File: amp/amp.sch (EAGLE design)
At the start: 77 parts, among them IC1 OPA2134PA, Q1 BC547, Q10 IRF540, Q11 BC556, Q12 BC556, Q13 BC547, Q14 BC547, Q15 2N7000, Q16 BC337, Q17 BC337, Q18 IRF540, Q19 IRF540, Q2 BC556, Q20 BC547, Q3 BC547, Q4 BC556, Q5 2N7000, Q6 BC337, Q7 BC337, Q8 BC547, Q9 IRF540

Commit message: MOSFET driver stage
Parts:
- removed C10, C9: 0.1uF, SparkFun-Capacitors:0.1UF-25V(+80/-20%)(0603)
- removed C7, C8: 82nF, SparkFun-Capacitors:1.0UF-25V-+80/-20(0805)"
- added Q21, Q22: BC547, transistor-npn:BC547
- added Q23, Q24: IRF540, transistor-power:IRF540
- Q10, Q18, Q19, Q9: value IRF540 -> BC547; device transistor-power:IRF540 -> transistor-npn:BC547
- Q11, Q12: value BC556 -> IRF540; device my:BC556 -> transistor-power:IRF540
- Q14: value BC547 -> BC556; device transistor-npn:BC547 -> my:BC556
- Q15: value 2N7000 -> BC547; device SparkFun-DiscreteSemi:MOSFET-NCHANNEL2N7000 -> transistor-npn:BC547
- Q16: value BC337 -> BC556; device transistor:BC337 -> my:BC556
- Q17: value BC337 -> 2N7000; device transistor:BC337 -> SparkFun-DiscreteSemi:MOSFET-NCHANNEL2N7000
- Q6, Q7: value BC337 -> BC547; device transistor:BC337 -> transistor-npn:BC547
- R11, R30: value 383 -> 120
- R12: value 2.2k -> 120
- R13: value 2.4 -> 549; device SparkFun-Resistors:RESISTORPTH-1/2W -> SparkFun-Resistors:RESISTORPTH-1/4W
- R14: value 1M -> 220
- R15: value 1M -> 2.2k
- R16: value 16k -> 2.4; device SparkFun-Resistors:RESISTORPTH-1/4W -> SparkFun-Resistors:RESISTORPTH-1/2W
- R17, R18: value 120 -> 1M
- R19: value 150 -> 4.7k
- R20: value 4.7k -> 120
- R21: value 2.2k -> 16k
- R22: value 120 -> 150
- R23, R5: value 120 -> 500; device SparkFun-Resistors:RESISTORPTH-1/4W -> SparkFun-Electromechanical:TRIMPOT3362U-2
- R24: value 2.4 -> 120; device SparkFun-Resistors:RESISTORPTH-1/2W -> SparkFun-Resistors:RESISTORPTH-1/4W
- R25: value 2.2k -> 2K
- R27: value 2K -> 2.61k
- R28, R29: value 1M -> 120
- R31: value 500 -> 549; device SparkFun-Electromechanical:TRIMPOT3362U-2 -> SparkFun-Resistors:RESISTORPTH-1/4W
- R32: value 500 -> 220; device SparkFun-Electromechanical:TRIMPOT3362U-2 -> SparkFun-Resistors:RESISTORPTH-1/4W
- R33: value 10 -> 2.2k
- R34: value 10 -> 2.4; device SparkFun-Resistors:RESISTORPTH-1/4W -> SparkFun-Resistors:RESISTORPTH-1/2W
- R35, R36: value 2.7 -> 1M
- R6: value 2K -> 120
- R7: value 10k -> 2K
- R8: value 2.2k -> 10k
- R9: value 120 -> 2.61k
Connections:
- new net N$45: Q7.E, Q8.C, R14.2
- new net N$46: Q20.E, R29.2
- net GND: now also C6.2, R18.2, R19.2, R25.1, R33.2, R36.2, R7.1, X3-2.KL; no longer C10.2, C5.2, C9.2, R12.2, R20.2, R25.2, R27.1, R29.2, R6.1, X4-2.KL
- net HIN: now also X4-2.KL; no longer X3-2.KL
- net HOUT: now also X4-1.KL; no longer X3-1.KL
- net HT: now also Q17.D, R20.2, R24.2, R6.2; no longer Q15.D, R17.2, R18.2, R5.2
- net INL: now also X3-1.KL; no longer X4-1.KL
- net N$10: now also Q8.B, Q9.B, Q9.C, R13.1; no longer Q7.B, Q7.C, R11.1
- net N$11: now also R10.2; no longer R9.2
- net N$12: now also Q9.E, R12.2; no longer Q7.E, R10.2
- net N$13: now also Q18.C, Q19.B, R27.1; no longer C7.2, Q6.C, R33.2, R8.1
- net N$14: now also R9.2; no longer C7.1, R8.2
- net N$15: now also Q10.C, Q12.G, R15.1; no longer Q10.G, Q8.C, R12.1
- net N$16: now also Q10.B, Q12.S, R16.2; no longer Q10.S, Q8.B, R13.2
- net N$17: now also R18.1; no longer R15.1
- net N$18: now also Q15.C; no longer Q13.C
- net N$19: now also R17.1; no longer R14.1
- net N$20: now also Q14.B, Q14.C, Q16.B, R21.2; no longer Q11.B, Q11.C, Q12.B, R16.2
- net N$21: now also R13.2; no longer R11.2
- net N$22: now also Q16.C, Q17.G; no longer Q12.C, Q15.G
- net N$23: now also R21.1; no longer R16.1
- net N$24: now also Q14.E, R20.1; no longer Q11.E, R17.1
- net N$25: now also Q16.E, R24.1; no longer Q12.E, R18.1
- net N$26: now also Q13.B, Q15.E, R22.2; no longer Q13.E, Q14.B, R19.2
- net N$27: now also Q13.C, Q15.B, R19.1; no longer Q13.B, Q14.C, R20.1
- net N$28: now also Q18.B, Q20.B, Q21.B, Q21.C, R31.1; no longer Q16.B, Q16.C, Q17.B, R30.1
- net N$29: now also Q18.E, R28.2; no longer Q17.E, R22.2
- net N$30: now also Q21.E, R30.2; no longer Q16.E, R23.2
- net N$31: now also Q19.E, Q20.C, R32.2; no longer C8.2, Q17.C, R21.1, R34.2
- net N$32: now also Q8.E, R11.2; no longer C8.1, Q15.S, R21.2
- net N$33: now also Q22.C, Q24.G, R33.1; no longer Q19.G, Q20.C, R25.1
- net N$34: now also Q22.B, Q24.S, R34.2; no longer Q19.S, Q20.B, R24.2
- net N$35: now also R25.2; no longer R27.2
- net N$36: now also C5.2, R36.1; no longer C6.2, R29.1
- net N$37: now also C6.1, R35.1; no longer C5.1, R28.1
- net N$38: now also C5.1, R31.2; no longer C6.1, R30.2
- net N$39: now also R5.CCW; no longer R31.CCW
- net N$40: now also R22.1, R23.CCW; no longer R19.1, R32.CCW
- net N$41: now also Q11.G, R14.1; no longer Q9.G, R33.1
- net N$42: now also Q23.G, R32.1; no longer Q18.G, R34.1
- net N$43: now also Q17.S, R27.2; no longer C9.1, R35.1
- net N$44: now also Q6.C, Q7.B, R9.1; no longer C10.1, R36.1
- net N$6: now also R6.1; no longer R5.1
- net N$9: now also R8.2; no longer R6.2
- net OUTL: now also Q11.S, Q12.D, R17.2, R8.1; no longer Q10.D, Q9.S, R14.2, R35.2, R7.1
- net OUTR: now also Q23.S, Q24.D, R35.2; no longer Q18.S, Q19.D, R28.2, R36.2
- net VCC: now also Q11.D, Q19.C, Q23.D, Q7.C; no longer Q18.D, Q9.D
- net VEE: now also Q10.E, Q13.E, Q22.E, R11.1, R12.1, R16.1, R23.CW, R23.WIPER, R28.1, R29.1, R30.1, R34.1, R5.CW, R5.WIPER; no longer Q14.E, Q20.E, Q8.E, R13.1, R22.1, R23.1, R24.1, R31.CW, R31.WIPER, R32.CW, R32.WIPER, R9.1
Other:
- note removed: "20mA"
- moved on the sheet: C1, C2, C3, C4, C5, C6, IC1A, IC1B, Q13, Q20, Q7, Q8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

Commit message: Gain switching jumper
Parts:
- added JP1, JP2: (no value), SparkFun-Retired:JUMPER-2PTH
- added R37, R38: 680, SparkFun-Resistors:RESISTORPTH-1/4W
- R25, R7: value 2K -> 2.7k
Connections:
- new net N$47: JP1.1, R37.1
- new net N$48: JP2.1, R38.1
- net GND: now also JP1.2, JP2.2
- net N$35: now also R38.2
- net N$9: now also R37.2
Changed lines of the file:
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@@
 <setting verticaltext="up"/>
 </settings>
-<grid distance="0.1" unitdist="inch" unit="inch" style="dots" multiple="1" display="yes" altdistance="0.01" altunitdist="inch" altunit="inch"/>
+<grid distance="0.1" unitdist="inch" unit="inch" style="lines" multiple="1" display="no" altdistance="0.01" altunitdist="inch" altunit="inch"/>
 <layers>
 <layer number="1" name="Top" color="4" fill="1" visible="no" active="no"/>
@@
 <part name="GND4" library="SparkFun-Aesthetics" deviceset="GND" device=""/>
 <part name="R8" library="SparkFun-Resistors" deviceset="RESISTOR" device="PTH-1/4W" value="10k"/>
-<part name="R7" library="SparkFun-Resistors" deviceset="RESISTOR" device="PTH-1/4W" value="2K"/>
+<part name="R7" library="SparkFun-Resistors" deviceset="RESISTOR" device="PTH-1/4W" value="2.7k"/>
 <part name="GND2" library="SparkFun-Aesthetics" deviceset="GND" device=""/>
 <part name="IC1" library="linear" deviceset="OPA2*" device="PA" technology="134"/>
@@
 <part name="GND10" library="SparkFun-Aesthetics" deviceset="GND" device=""/>
 <part name="R26" library="SparkFun-Resistors" deviceset="RESISTOR" device="PTH-1/4W" value="10k"/>
-<part name="R25" library="SparkFun-Resistors" deviceset="RESISTOR" device="PTH-1/4W" value="2K"/>
+<part name="R25" library="SparkFun-Resistors" deviceset="RESISTOR" device="PTH-1/4W" value="2.7k"/>
 <part name="GND9" library="SparkFun-Aesthetics" deviceset="GND" device=""/>
 <part name="R35" library="SparkFun-Resistors" deviceset="RESISTOR" device="PTH-1/4W" value="1M"/>
@@
 <part name="R29" library="SparkFun-Resistors" deviceset="RESISTOR" device="PTH-1/4W" value="120"/>
 <part name="Q19" library="transistor-npn" deviceset="BC547*" device=""/>
+<part name="R37" library="SparkFun-Resistors" deviceset="RESISTOR" device="PTH-1/4W" value="680"/>
+<part name="GND13" library="SparkFun-Aesthetics" deviceset="GND" device=""/>
+<part name="JP1" library="SparkFun-Retired" deviceset="JUMPER-2" device="PTH"/>
+<part name="R38" library="SparkFun-Resistors" deviceset="RESISTOR" device="PTH-1/4W" value="680"/>
+<part name="GND14" library="SparkFun-Aesthetics" deviceset="GND" device=""/>
+<part name="JP2" library="SparkFun-Retired" deviceset="JUMPER-2" device="PTH"/>
 </parts>
 <sheets>
@@
 <instance part="R11" gate="G$1" x="111.76" y="106.68" rot="R90"/>
 <instance part="Q7" gate="G$1" x="109.22" y="137.16"/>
+<instance part="R37" gate="G$1" x="71.12" y="116.84" rot="R270"/>
+<instance part="GND13" gate="1" x="83.82" y="116.84"/>
+<instance part="JP1" gate="A" x="76.2" y="124.46"/>
 </instances>
 <busses>
@@
 <wire x1="243.84" y1="88.9" x2="246.38" y2="88.9" width="0.1524" layer="91"/>
 <label x="246.38" y="88.9" size="1.778" layer="95" xref="yes"/>
+</segment>
+<segment>
+<pinref part="JP1" gate="A" pin="2"/>
+<pinref part="GND13" gate="1" pin="GND"/>
+<wire x1="78.74" y1="121.92" x2="83.82" y2="121.92" width="0.1524" layer="91"/>
+<wire x1="83.82" y1="121.92" x2="83.82" y2="119.38" width="0.1524" layer="91"/>
 </segment>
 </net>
@@
 <wire x1="71.12" y1="109.22" x2="71.12" y2="104.14" width="0.1524" layer="91"/>
 <junction x="71.12" y="109.22"/>
+<pinref part="R37" gate="G$1" pin="2"/>
+<wire x1="71.12" y1="109.22" x2="71.12" y2="111.76" width="0.1524" layer="91"/>
 </segment>
 </net>
@@
 <pinref part="R14" gate="G$1" pin="2"/>
 <wire x1="116.84" y1="152.4" x2="152.4" y2="152.4" width="0.1524" layer="91"/>
+</segment>
+</net>
+<net name="N$47" class="0">
+<segment>
+<pinref part="R37" gate="G$1" pin="1"/>
+<pinref part="JP1" gate="A" pin="1"/>
+<wire x1="71.12" y1="121.92" x2="76.2" y2="121.92" width="0.1524" layer="91"/>
 </segment>
 </net>
@@
 <instance part="R29" gate="G$1" x="139.7" y="111.76" rot="R90"/>
 <instance part="Q19" gate="G$1" x="137.16" y="142.24"/>
+<instance part="R38" gate="G$1" x="99.06" y="121.92" rot="R270"/>
+<instance part="GND14" gate="1" x="111.76" y="121.92"/>
+<instance part="JP2" gate="A" x="104.14" y="129.54"/>
 </instances>
 <busses>
@@
 <wire x1="213.36" y1="38.1" x2="213.36" y2="35.56" width="0.1524" layer="91"/>
 <pinref part="GND11" gate="1" pin="GND"/>
+</segment>
+<segment>
+<pinref part="JP2" gate="A" pin="2"/>
+<pinref part="GND14" gate="1" pin="GND"/>
+<wire x1="106.68" y1="127" x2="111.76" y2="127" width="0.1524" layer="91"/>
+<wire x1="111.76" y1="127" x2="111.76" y2="124.46" width="0.1524" layer="91"/>
 </segment>
 </net>
@@
 <wire x1="99.06" y1="114.3" x2="99.06" y2="109.22" width="0.1524" layer="91"/>
 <junction x="99.06" y="114.3"/>
+<pinref part="R38" gate="G$1" pin="2"/>
+<wire x1="99.06" y1="114.3" x2="99.06" y2="116.84" width="0.1524" layer="91"/>
 </segment>
 </net>
@@
 </segment>
 </net>
+<net name="N$48" class="0">
+<segment>
+<pinref part="R38" gate="G$1" pin="1"/>
+<pinref part="JP2" gate="A" pin="1"/>
+<wire x1="99.06" y1="127" x2="104.14" y2="127" width="0.1524" layer="91"/>
+</segment>
+</net>

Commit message: CM degeneration values lowered
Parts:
- R10, R11, R12, R28, R29, R30: value 120 -> 56
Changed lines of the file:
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@@
 <?xml version="1.0" encoding="utf-8"?>
 <!DOCTYPE eagle SYSTEM "eagle.dtd">
-<eagle version="7.6.0">
+<eagle version="7.7.0">
 <drawing>
 <settings>
@@
 <part name="Q9" library="transistor-npn" deviceset="BC547*" device=""/>
 <part name="Q6" library="transistor-npn" deviceset="BC547*" device=""/>
-<part name="R10" library="SparkFun-Resistors" deviceset="RESISTOR" device="PTH-1/4W" value="120"/>
-<part name="R12" library="SparkFun-Resistors" deviceset="RESISTOR" device="PTH-1/4W" value="120"/>
+<part name="R10" library="SparkFun-Resistors" deviceset="RESISTOR" device="PTH-1/4W" value="56"/>
+<part name="R12" library="SparkFun-Resistors" deviceset="RESISTOR" device="PTH-1/4W" value="56"/>
 <part name="Q11" library="transistor-power" deviceset="IRF540" device=""/>
 <part name="Q12" library="transistor-power" deviceset="IRF540" device=""/>
@@
 <part name="Q21" library="transistor-npn" deviceset="BC547*" device=""/>
 <part name="Q18" library="transistor-npn" deviceset="BC547*" device=""/>
-<part name="R28" library="SparkFun-Resistors" deviceset="RESISTOR" device="PTH-1/4W" value="120"/>
-<part name="R30" library="SparkFun-Resistors" deviceset="RESISTOR" device="PTH-1/4W" value="120"/>
+<part name="R28" library="SparkFun-Resistors" deviceset="RESISTOR" device="PTH-1/4W" value="56"/>
+<part name="R30" library="SparkFun-Resistors" deviceset="RESISTOR" device="PTH-1/4W" value="56"/>
 <part name="Q23" library="transistor-power" deviceset="IRF540" device=""/>
 <part name="Q24" library="transistor-power" deviceset="IRF540" device=""/>
@@
 <part name="R32" library="SparkFun-Resistors" deviceset="RESISTOR" device="PTH-1/4W" value="220"/>
 <part name="Q8" library="transistor-npn" deviceset="BC547*" device=""/>
-<part name="R11" library="SparkFun-Resistors" deviceset="RESISTOR" device="PTH-1/4W" value="120"/>
+<part name="R11" library="SparkFun-Resistors" deviceset="RESISTOR" device="PTH-1/4W" value="56"/>
 <part name="Q7" library="transistor-npn" deviceset="BC547*" device=""/>
 <part name="Q20" library="transistor-npn" deviceset="BC547*" device=""/>
-<part name="R29" library="SparkFun-Resistors" deviceset="RESISTOR" device="PTH-1/4W" value="120"/>
+<part name="R29" library="SparkFun-Resistors" deviceset="RESISTOR" device="PTH-1/4W" value="56"/>
 <part name="Q19" library="transistor-npn" deviceset="BC547*" device=""/>
 <part name="R37" library="SparkFun-Resistors" deviceset="RESISTOR" device="PTH-1/4W" value="680"/>

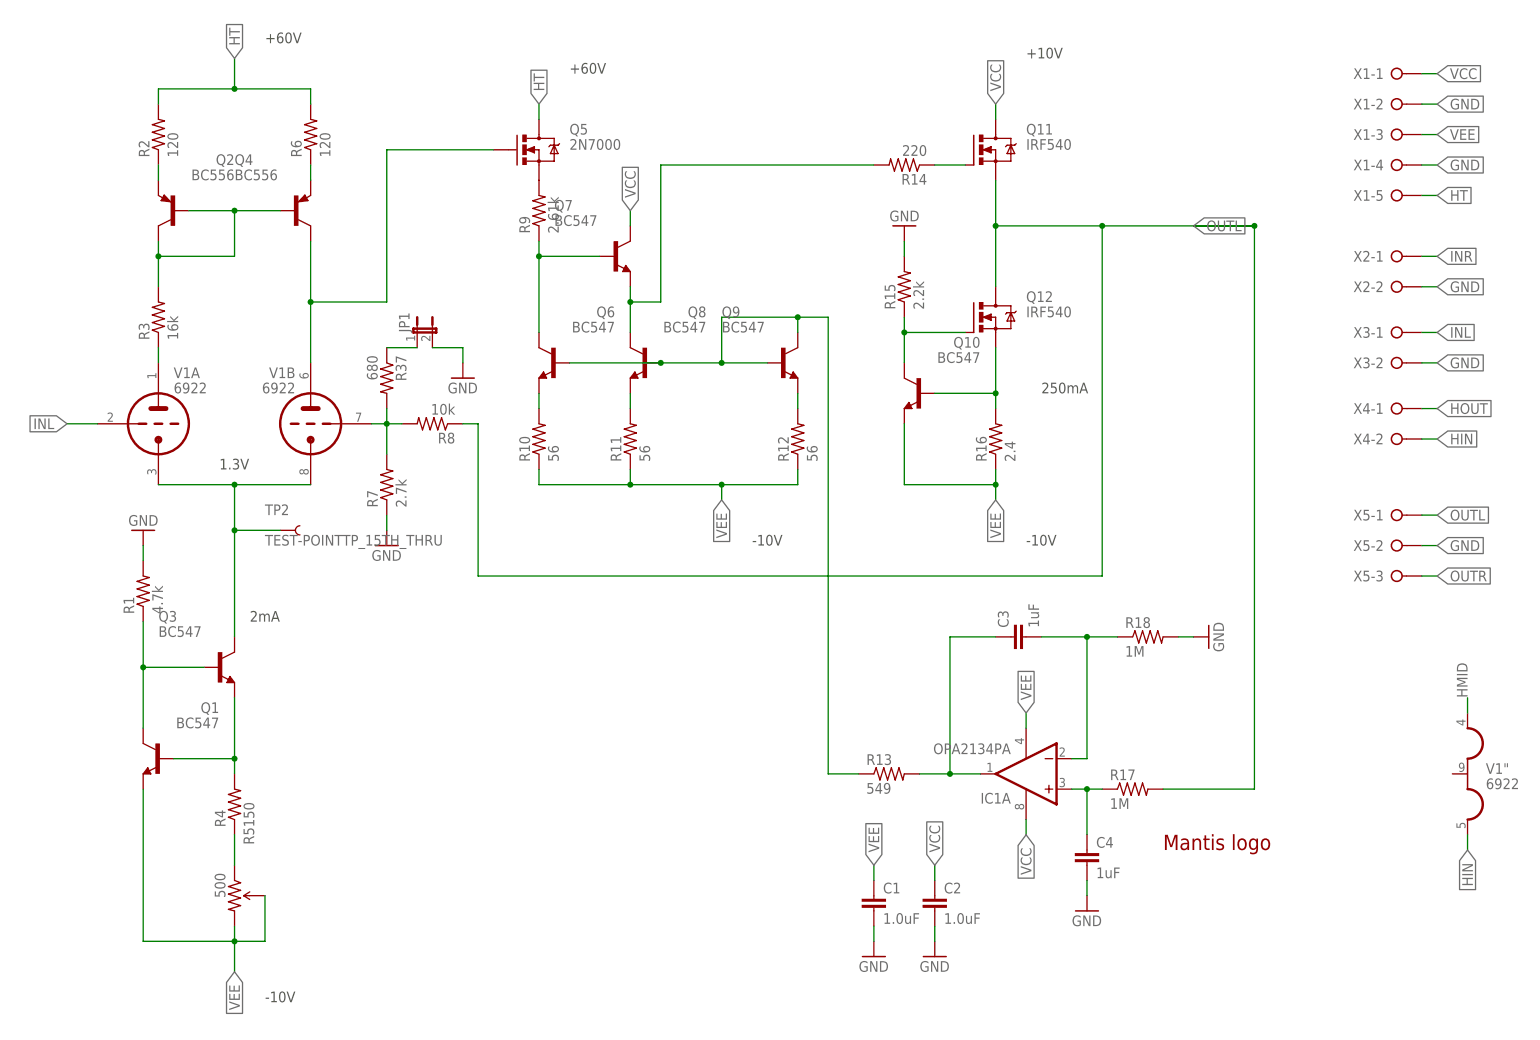
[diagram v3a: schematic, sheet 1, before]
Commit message: Some components changed
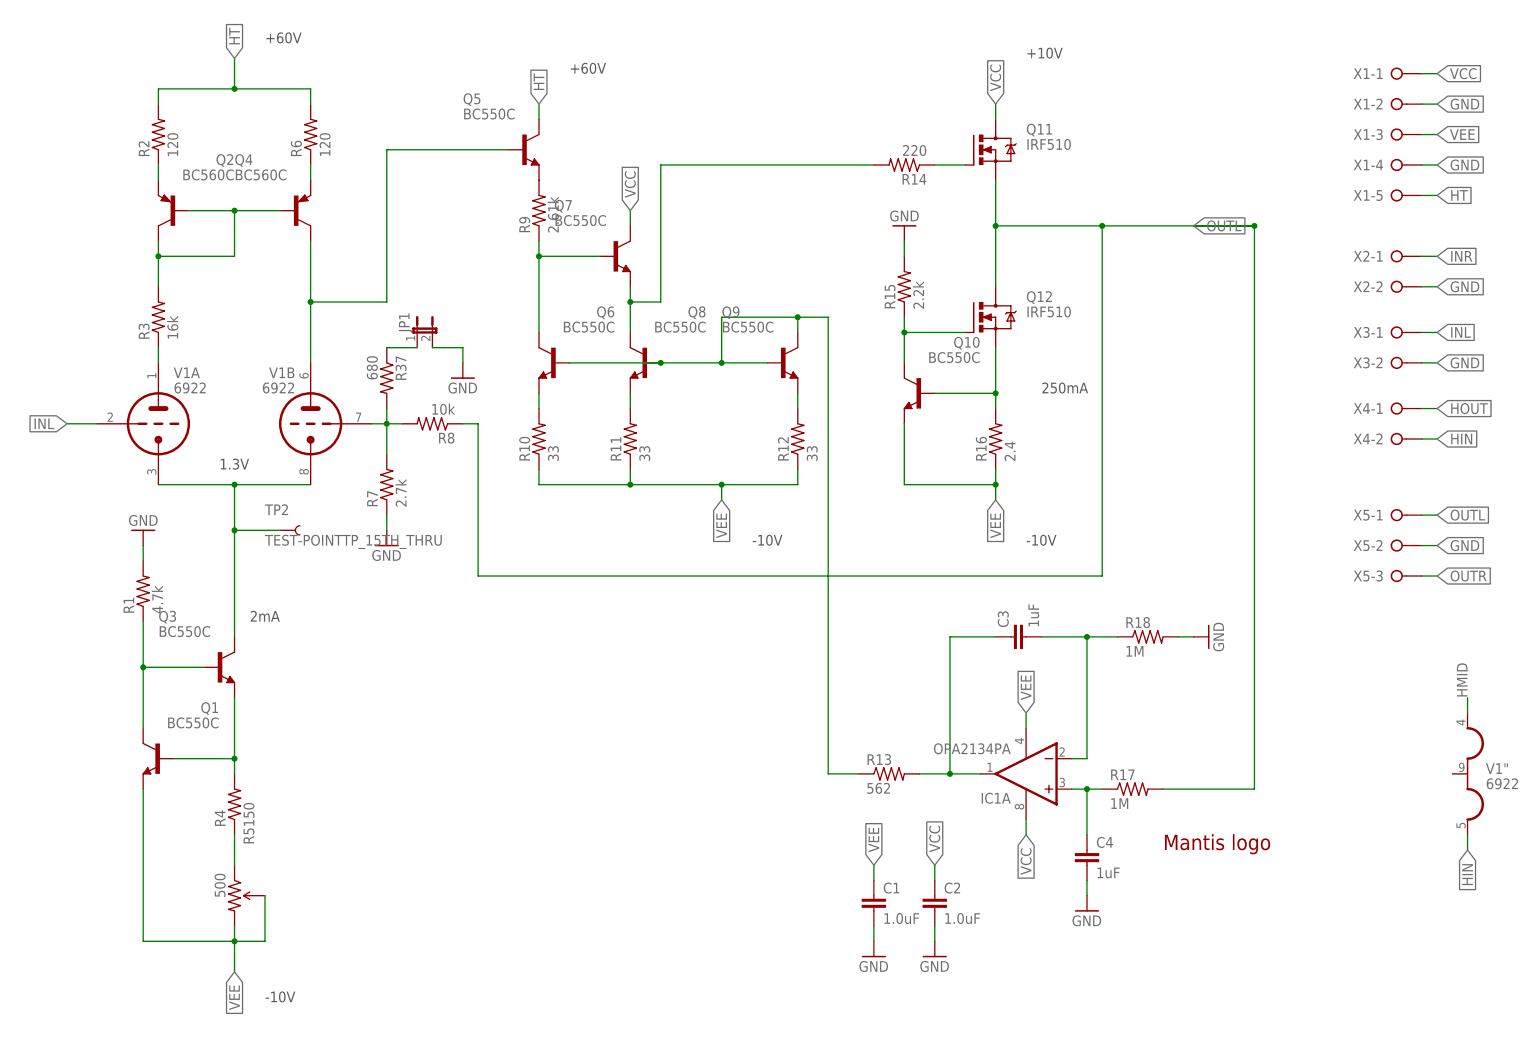
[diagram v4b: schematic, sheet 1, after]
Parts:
- Q1, Q10, Q13, Q15, Q18, Q19, Q20, Q21, Q22, Q3, Q6, Q7, Q8, Q9: value BC547 -> BC550C
- Q11, Q12, Q23, Q24: value IRF540 -> IRF510
- Q14, Q16, Q2, Q4: value BC556 -> BC560C
- Q17, Q5: value 2N7000 -> BC550C; device SparkFun-DiscreteSemi:MOSFET-NCHANNEL2N7000 -> transistor-npn:BC547
- R10, R11, R12, R28, R29, R30: value 56 -> 33
- R13, R31: value 549 -> 562
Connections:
- net HT: now also Q17.C, Q5.C; no longer Q17.D, Q5.D
- net N$14: now also Q5.E; no longer Q5.S
- net N$22: now also Q17.B; no longer Q17.G
- net N$4: now also Q5.B; no longer Q5.G
- net N$43: now also Q17.E; no longer Q17.S
